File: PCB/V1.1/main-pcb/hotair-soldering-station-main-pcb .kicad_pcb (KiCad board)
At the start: 2 copper layers, 89.4 x 90.9 mm, 95 parts, among them J1 230VAC_IN, J10 SOLD_IRON (r.2,54), J11 LCD_CON2 (JST r.2.0), J12 LCD_CON1 (JST r.2.0), J13 ICP (goldpin r2,54), J2 FRONT_PANEL (IDC r. 2,54), J3 EARTH_GND, J4 24V_IN (NS-25 r2,54), J5 PSUPPLY (PWZ-02S r.3,96), J6 HOTAIR_FAN (JST r,2,54), J7 HOTAIR_MEAS (JST r.2,5), J8 HOTAIR_HEATER (PWZ-02S r.3,96), J9 SOLD_IRON (r.2,54), Q1 BC817, Q10 FP3055LP, Q11 BC817, Q2 BC807, Q3 BC817, Q4 Q_PMOS_GDS, Q5 BC817, Q6 BT139-600, Q7 BC817, Q8 FP3055LP, Q9 BC817, U1 MOC3041M, U2 MAX31855KASA, U3 MP1584-Step-Down, U4 AP1117-ADJ, U6 LM358, U7 MAX31855KASA, U8 STM32F103C6Tx

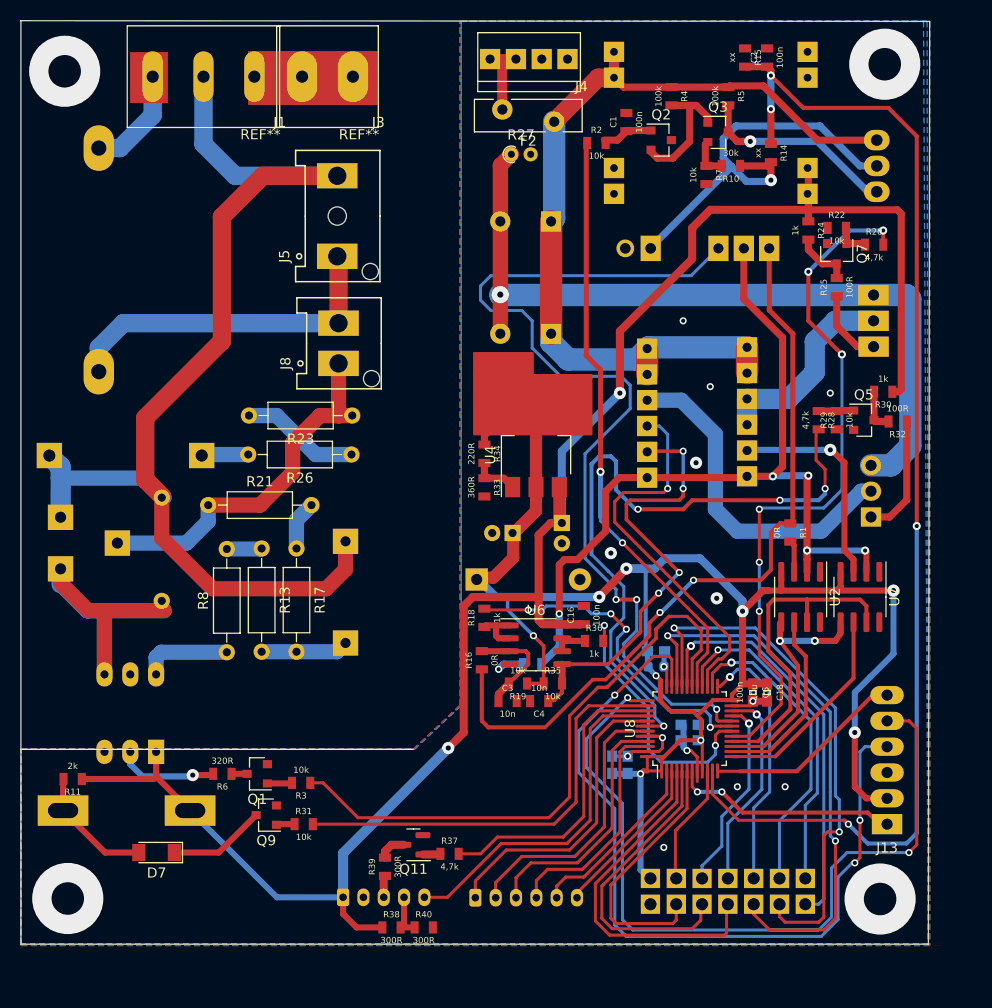
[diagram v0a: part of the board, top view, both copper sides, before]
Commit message: Front panel V2, PCB text alignment, drill resize, T12 connector split
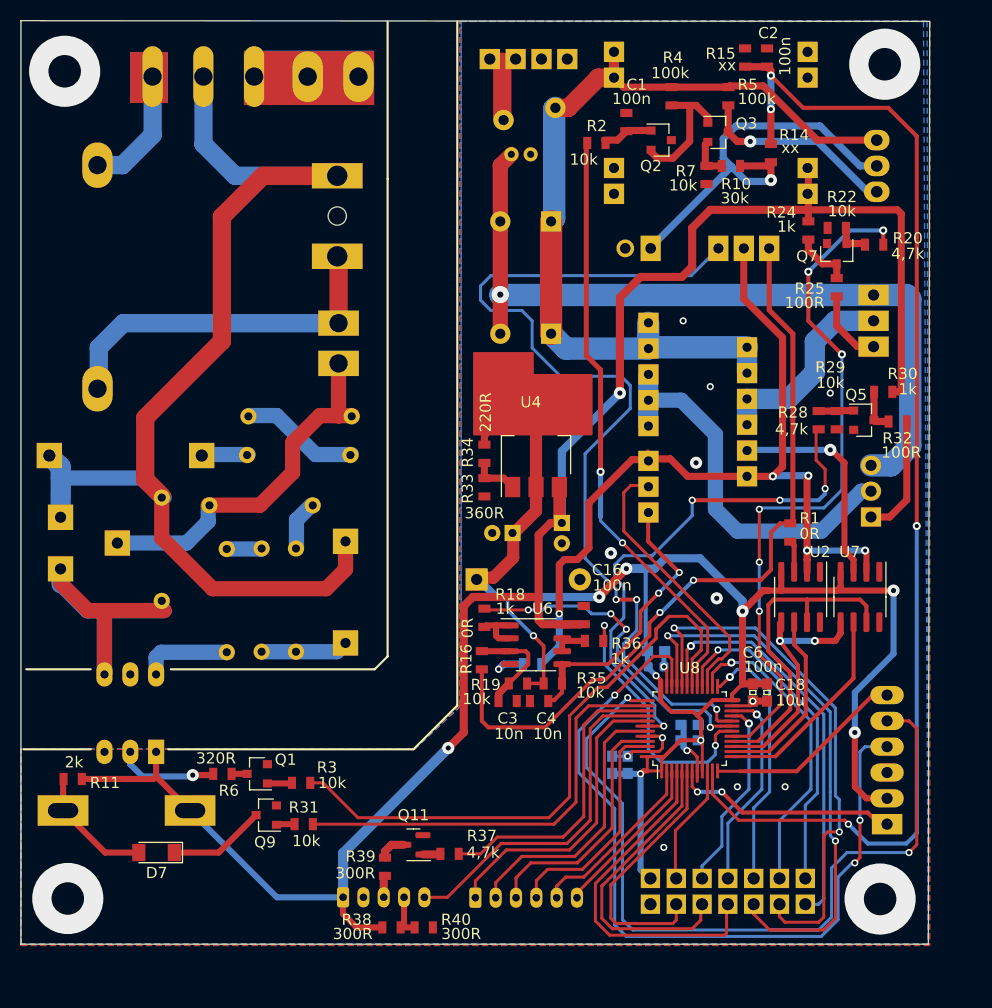
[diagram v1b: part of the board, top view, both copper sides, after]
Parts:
- added J14: T12_signal (NS-25 r2,54), Connector:Conn-01x03-N25-W4P, B.Cu at (75.6, 59.9)
- F2, J1, J13, J3, J4, J5, J8, R13, R17, R21, R23, R26, R27, R8: moved to B.Cu
- J10: value SOLD_IRON (r.2,54) -> T12_power (NS-25 r2,54); footprint My-Footprints:Conn_1x06 -> Connector:Conn-01x05-N25-W4P
- J9: value SOLD_IRON (r.2,54) -> WEP (r.2,54)
- moved J1 10.0 mm to (42.5, 18.5)
- moved J3 9.45 mm to (42.7, 28.5), turned to 0 degrees
- moved J4 6.40 mm to (72.1, 18.5)
- moved J10 2.64 mm to (75.6, 46.3)
- moved F1 1.68 mm to (24.5, 54.2)
- moved F2 1.37 mm to (69.6, 26.5)
- moved R21 0.13 mm to (35.6, 65.7)
- moved R26 0.12 mm to (49.4, 60.7)
- moved R23 0.09 mm to (49.5, 56.9)
- moved R17 0.05 mm to (44.1, 69.9)
- turned J13 to 0 degrees
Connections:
- J10 pad 4: IRON_T12_MOTION_SW -> IRON_T12_HEATER
- J10 pad 5: IRON_T12_THERM -> IRON_T12_HEATER
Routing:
- net IRON_T12_THERM: track 43.8 -> 28.3 mm, vias 4 -> 2
- net IRON_T12_HEATER_CTRL: track 67.0 -> 52.9 mm
- net IRON_T12_MOTION_SW: track 37.4 -> 27.2 mm, vias 1 -> 0
- net Net-(F2-Pad2): track 7.87 -> 13.7 mm
- net IRON_T12_HEATER: track 33.3 -> 38.4 mm
- net +5V: track 180.9 -> 183.3 mm
- net THERM_GND: track 83.1 -> 85.1 mm
- net Net-(F1-Pad2): track 10.4 -> 12.4 mm
- net AC_230(L): track 33.6 -> 35.3 mm
- net +24V: track 86.1 -> 85.4 mm
- net Net-(J1-Pad1): track 10.8 -> 10.3 mm
- net GND: vias 16 -> 18
- net (no net): vias 3 -> 1
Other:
- board text added: "230V INPUT"
- board text added: "24V IN"
- board text added: "EARTH"
- board text added: "FRONT PANEL"
- board text added: "FUSE: 1,6A"
- board text added: "HOTAIR FAN"
- board text added: "HOTAIR HEATER"
- board text added: "HOTAIR SIGNAL"
- board text added: "ICP"
- board text added: "LCD CON1"
- board text added: "LCD CON2"
- board text added: "POWER SUPPLY 230v MAINS"
- board text added: "T12 POWER"
- board text added: "T12 SIGNAL"
- board text added: "WEP"

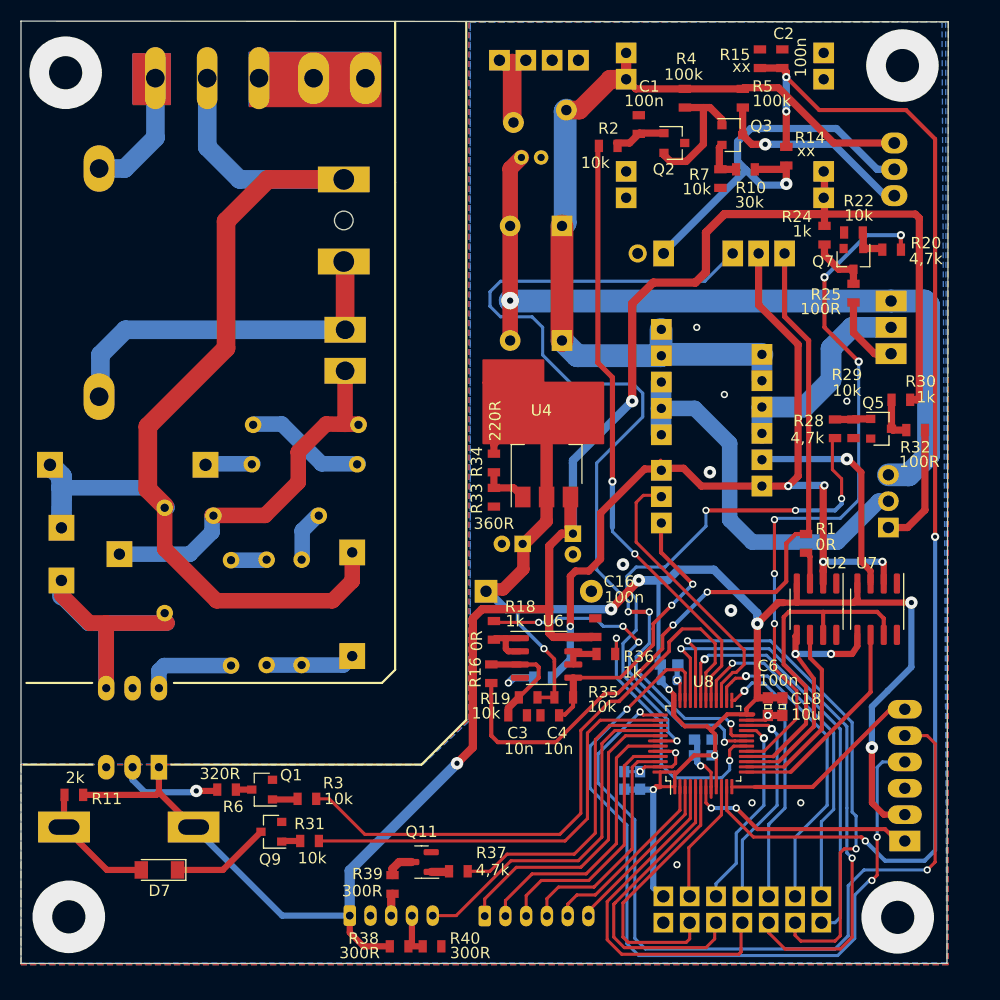
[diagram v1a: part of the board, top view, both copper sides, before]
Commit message: Fixing DRC violations
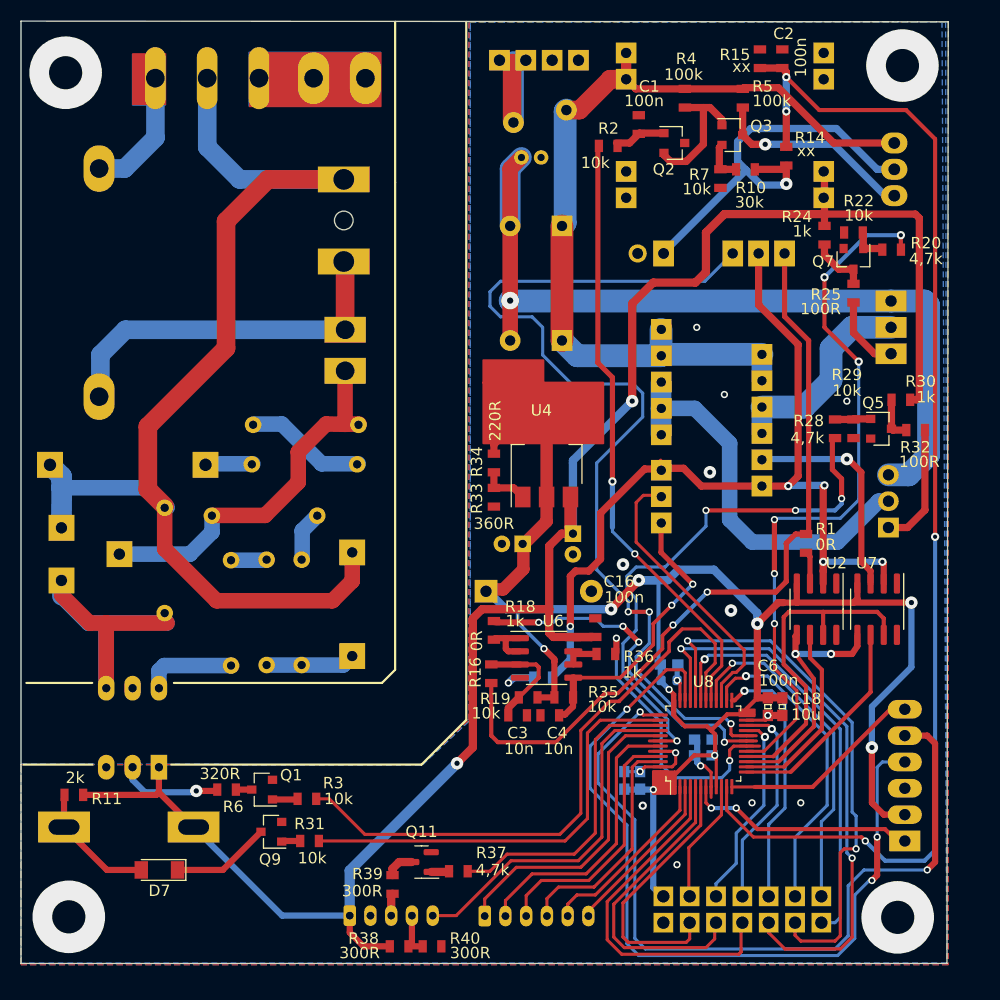
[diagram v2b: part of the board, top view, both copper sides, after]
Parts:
- moved R21 0.15 mm to (35.4, 65.7)
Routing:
- net Net-(F2-Pad2): track 13.7 -> 23.3 mm
- net GND2: track 77.8 -> 84.8 mm
- net UART_DBG_TX: track 21.1 -> 18.4 mm
- net IRON_T12_TEMP_ADC: track 26.7 -> 27.8 mm
- net GND: track 26.1 -> 25.1 mm, vias 18 -> 19
- net HOTAIR_REED_SW: track 92.3 -> 93.2 mm
- net Net-(Q3-Pad3): track 19.7 -> 18.8 mm
- net HOTAIR_TEMP_ADC: track 33.2 -> 34.0 mm
- net RST: track 22.3 -> 21.5 mm
- net MENU_DOWN_SW: track 25.9 -> 25.2 mm

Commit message: PCB silkscreen progress, remove DRC violations
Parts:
- added G***: LOGO, graphic:high-voltage, F.Cu at (56.3, 25.8)
- added G***: LOGO, graphic:high-voltage, F.Cu at (56.4, 72.9)
- added G***: LOGO, graphic:high-voltage, B.Cu at (56.8, 26.3)
- added G***: LOGO, graphic:high-voltage, B.Cu at (56.6, 72.9)
- added G***: LOGO, graphic:honeybadger2, B.Cu at (45.1, 93.6)
- Q10, Q8: footprint Package_TO_SOT_THT:TO-220-3_Vertical -> My-Footprints:TO-220-3_V_Thick_Pads
- Q4: footprint Power_Integrations:TO-220 -> My-Footprints:TO-220-3_V_Thick_Pads
- Q6: footprint My-Footprints:TO-220-3_Vertical -> My-Footprints:TO-220-3_V_Wide_Legs
- moved Q4 2.44 mm to (101.1, 34.7)
- moved Q10 0.82 mm to (101.5, 66.8)
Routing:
- net FAN_SUPPLY: track 41.1 -> 42.6 mm
- net IRON_T12_HEATER: track 38.4 -> 39.2 mm
- net GND2: track 84.8 -> 84.0 mm
- net Net-(Q3-Pad3): track 18.8 -> 19.5 mm
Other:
- board text added: "MAIN PCB V1.1 02.2021"
- board text added: "SHW-01 HOTAIR/SOLDERING STATION"
- board text added: "WARNING! MAINS VOLTAGE!"

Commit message: Main PCB in production! Generate gerber, add silkscreen logos, expose cu on high current traces, some other minor refinements
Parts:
- added G***: LOGO, graphic:open-source-HW-10x10, B.Cu at (95.2, 77.0)
- moved G*** 0.59 mm to (56.7, 26.2), turned to -90 degrees
- moved G*** 0.20 mm to (56.6, 72.9), turned to -90 degrees
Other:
- board size 89.4 x 90.9 mm -> 90 x 91 mm

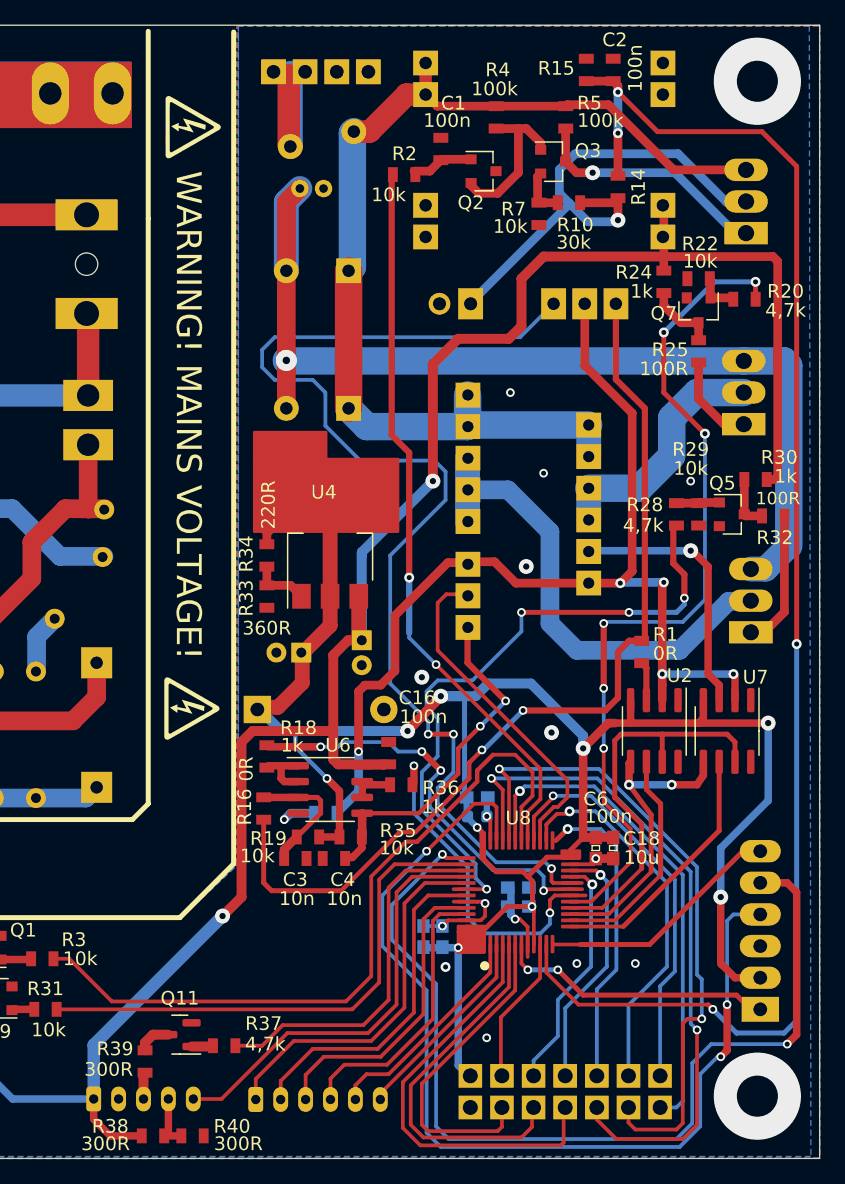
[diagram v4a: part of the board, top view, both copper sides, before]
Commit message: Configure STM32F1 uC. Fix reset pin and UART problems.
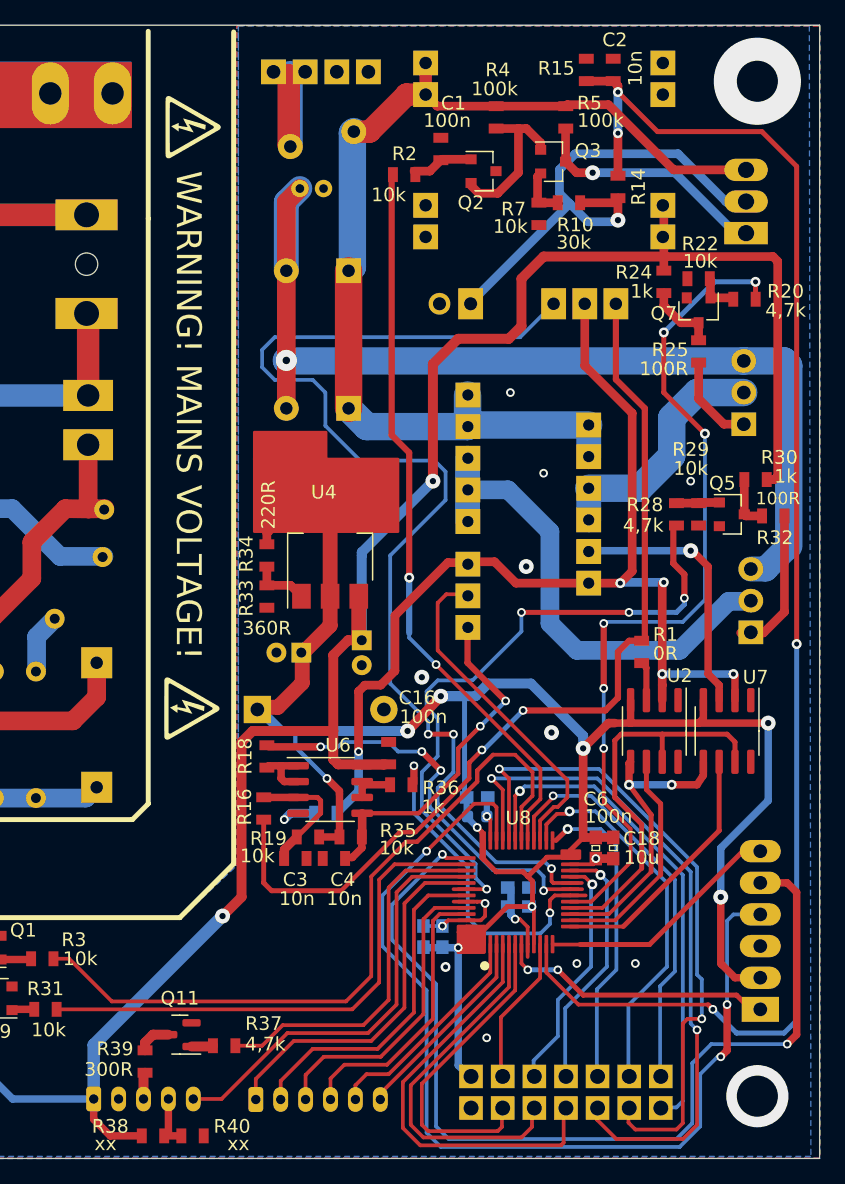
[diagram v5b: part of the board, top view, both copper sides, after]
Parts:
- C2: value 100n -> 10n
- J2: footprint My-Footprints:Conn-01x14 -> My-Footprints:Conn-01x14-IDC
- Q10, Q8: footprint My-Footprints:TO-220-3_V_Thick_Pads -> Package_TO_SOT_THT:TO-220-3_Vertical
- R38, R40: value 300R -> xx
- moved J2 9.98 mm to (73.7, 91.2)
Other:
- board text added: "MAIN PCB V1.1 02.2022"
- board text removed: "MAIN PCB V1.1 02.2021"
